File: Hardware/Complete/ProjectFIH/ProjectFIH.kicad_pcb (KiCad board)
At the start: 2 copper layers, 94 x 99.1 mm, 84 parts, among them J1 Conn_01x02_Male, J10 Payload LED, J2 Power, J3 Power LED, J4 MCU Fail LED, J5 Heater LED, J6 Heater, J7 UART, J8 AVR-ISP-10, J9 Payload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

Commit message: Small PCB optimization
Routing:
- net Net-(C5-Pad1): track 71.5 -> 68.6 mm

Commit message: Small corrections
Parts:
- added R27: 470, Resistor_SMD:R_0805_2012Metric_Pad1.15x1.40mm_HandSolder, F.Cu at (75.2, 81.5)
- DA1: value LM335 -> LM135
- R15, R21: value 4.2k -> 4.3k
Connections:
- D5 pad 2: IRQ -> Net-(D5-Pad2)
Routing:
- net IRQ: track 43.3 -> 39.5 mm
- net Net-(D5-Pad2): track 0.00 -> 2.30 mm
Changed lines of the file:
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@@
     (thickness 1.6)
     (drawings 4)
-    (tracks 794)
+    (tracks 796)
     (zones 0)
-    (modules 84)
-    (nets 85)
+    (modules 85)
+    (nets 86)
   )
   (page A4)
@@
   (net 83 "Net-(U8-Pad27)")
   (net 84 "Net-(U8-Pad28)")
+  (net 85 "Net-(D5-Pad2)")
   (net_class Default "This is the default net class."
     (clearance 0.2)
@@
     (add_net "Net-(D4-Pad1)")
     (add_net "Net-(D5-Pad1)")
+    (add_net "Net-(D5-Pad2)")
     (add_net "Net-(D6-Pad1)")
     (add_net "Net-(DA1-Pad1)")
@@
     (add_net Temperature)
   )
+  (module Resistor_SMD:R_0805_2012Metric_Pad1.15x1.40mm_HandSolder (layer F.Cu)
+    (at 75.175 81.534)
+    (descr "Resistor SMD 0805 (2012 Metric), square (rectangular) end terminal, IPC_7351 nominal with elongated pad for handsoldering. (Body size source: https://docs.google.com/spreadsheets/d/1BsfQQcO9C6DZCsRaXUlFlo91Tg2WpOkGARC1WS5S8t0/edit?usp=sharing), generated with kicad-footprint-generator")
+    (tags "resistor handsolder")
+    (attr smd)
+    (fp_text reference R27 (at 0 -1.65) (layer F.SilkS)
+      (effects (font (size 1 1) (thickness 0.15)))
+    )
+    (fp_text value 470 (at 0 1.65) (layer F.Fab)
+      (effects (font (size 1 1) (thickness 0.15)))
+    )
+    (fp_text user %R (at 0 0) (layer F.Fab)
+      (effects (font (size 0.5 0.5) (thickness 0.08)))
+    )
+    (fp_line (start -1 0.6) (end -1 -0.6) (layer F.Fab) (width 0.1))
+    (fp_line (start -1 -0.6) (end 1 -0.6) (layer F.Fab) (width 0.1))
+    (fp_line (start 1 -0.6) (end 1 0.6) (layer F.Fab) (width 0.1))
+    (fp_line (start 1 0.6) (end -1 0.6) (layer F.Fab) (width 0.1))
+    (fp_line (start -0.261252 -0.71) (end 0.261252 -0.71) (layer F.SilkS) (width 0.12))
+    (fp_line (start -0.261252 0.71) (end 0.261252 0.71) (layer F.SilkS) (width 0.12))
+    (fp_line (start -1.85 0.95) (end -1.85 -0.95) (layer F.CrtYd) (width 0.05))
+    (fp_line (start -1.85 -0.95) (end 1.85 -0.95) (layer F.CrtYd) (width 0.05))
+    (fp_line (start 1.85 -0.95) (end 1.85 0.95) (layer F.CrtYd) (width 0.05))
+    (fp_line (start 1.85 0.95) (end -1.85 0.95) (layer F.CrtYd) (width 0.05))
+    (pad 2 smd roundrect (at 1.025 0) (size 1.15 1.4) (layers F.Cu F.Paste F.Mask) (roundrect_rratio 0.217391)
+      (net 85 "Net-(D5-Pad2)"))
+    (pad 1 smd roundrect (at -1.025 0) (size 1.15 1.4) (layers F.Cu F.Paste F.Mask) (roundrect_rratio 0.217391)
+      (net 20 IRQ))
+    (model ${KISYS3DMOD}/Resistor_SMD.3dshapes/R_0805_2012Metric.wrl
+      (at (xyz 0 0 0))
+      (scale (xyz 1 1 1))
+      (rotate (xyz 0 0 0))
+    )
+  )
   (module Capacitor_SMD:C_0805_2012Metric_Pad1.15x1.40mm_HandSolder (layer F.Cu)
     (at 46.745 36.322)
@@
       (net 19 "Net-(D5-Pad1)"))
     (pad 2 smd roundrect (at 1.4 0 180) (size 1.25 2.65) (layers F.Cu F.Paste F.Mask) (roundrect_rratio 0.2)
-      (net 20 IRQ))
+      (net 85 "Net-(D5-Pad2)"))
     (model ${KISYS3DMOD}/Diode_SMD.3dshapes/D_1210_3225Metric.wrl
       (at (xyz 0 0 0))
@@
       (effects (font (size 1 1) (thickness 0.15)) (justify mirror))
     )
-    (fp_text value LM335 (at 1.27 -2.79) (layer B.Fab)
+    (fp_text value LM135 (at 1.27 -2.79) (layer B.Fab)
       (effects (font (size 1 1) (thickness 0.15)) (justify mirror))
     )
@@
       (effects (font (size 1 1) (thickness 0.15)))
     )
-    (fp_text value 4.2k (at 0 1.65 90) (layer F.Fab)
+    (fp_text value 4.3k (at 0 1.65 90) (layer F.Fab)
       (effects (font (size 1 1) (thickness 0.15)))
     )
@@
       (effects (font (size 1 1) (thickness 0.15)))
     )
-    (fp_text value 4.2k (at 0 1.65 90) (layer F.Fab)
+    (fp_text value 4.3k (at 0 1.65 90) (layer F.Fab)
       (effects (font (size 1 1) (thickness 0.15)))
     )
@@
   (segment (start 61.976 82.296) (end 61.976 82.296) (width 0.5) (layer B.Cu) (net 20))
   (via (at 61.976 82.296) (size 2.54) (drill 0.5) (layers F.Cu B.Cu) (net 20))
-  (segment (start 77.972 82.804) (end 74.676 82.804) (width 0.5) (layer F.Cu) (net 20))
-  (segment (start 74.676 82.804) (end 73.406 81.534) (width 0.5) (layer F.Cu) (net 20))
   (segment (start 62.738 81.534) (end 61.976 82.296) (width 0.5) (layer F.Cu) (net 20))
-  (segment (start 73.406 81.534) (end 62.738 81.534) (width 0.5) (layer F.Cu) (net 20))
   (segment (start 61.976 82.296) (end 61.976 77.978) (width 0.5) (layer F.Cu) (net 20))
+  (segment (start 72.898 81.534) (end 62.738 81.534) (width 0.5) (layer F.Cu) (net 20))
+  (segment (start 73.406 81.534) (end 72.898 81.534) (width 0.5) (layer F.Cu) (net 20))
+  (segment (start 72.898 81.534) (end 74.15 81.534) (width 0.5) (layer F.Cu) (net 20))
   (segment (start 100.457 21.965) (end 100.457 20.075) (width 1) (layer F.Cu) (net 21))
   (segment (start 100.457 20.075) (end 100.212 20.075) (width 1) (layer F.Cu) (net 21))
@@
   (segment (start 68.132001 89.601999) (end 67.564 90.17) (width 1) (layer B.Cu) (net 58))
   (segment (start 81.727999 89.601999) (end 75.625001 89.601999) (width 0.5) (layer B.Cu) (net 58))
+  (segment (start 77.47 82.804) (end 76.2 81.534) (width 0.5) (layer F.Cu) (net 85))
+  (segment (start 77.972 82.804) (end 77.47 82.804) (width 0.5) (layer F.Cu) (net 85))
   (zone (net 4) (net_name GND) (layer F.Cu) (hatch edge 0.508)
     (connect_pads (clearance 0.508))

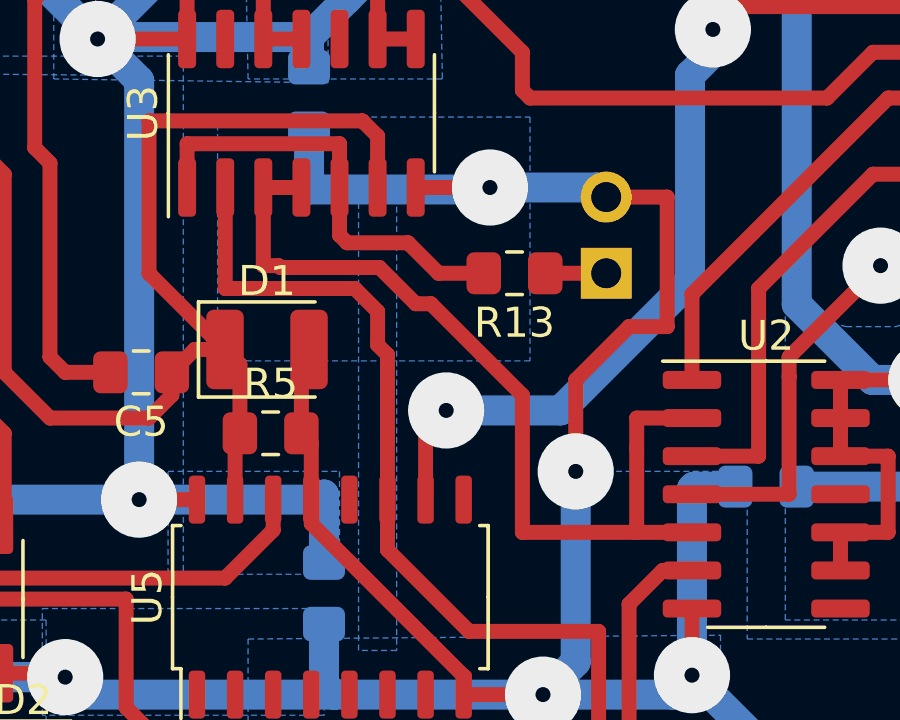
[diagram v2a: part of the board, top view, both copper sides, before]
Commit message: Swapped outputs of U3
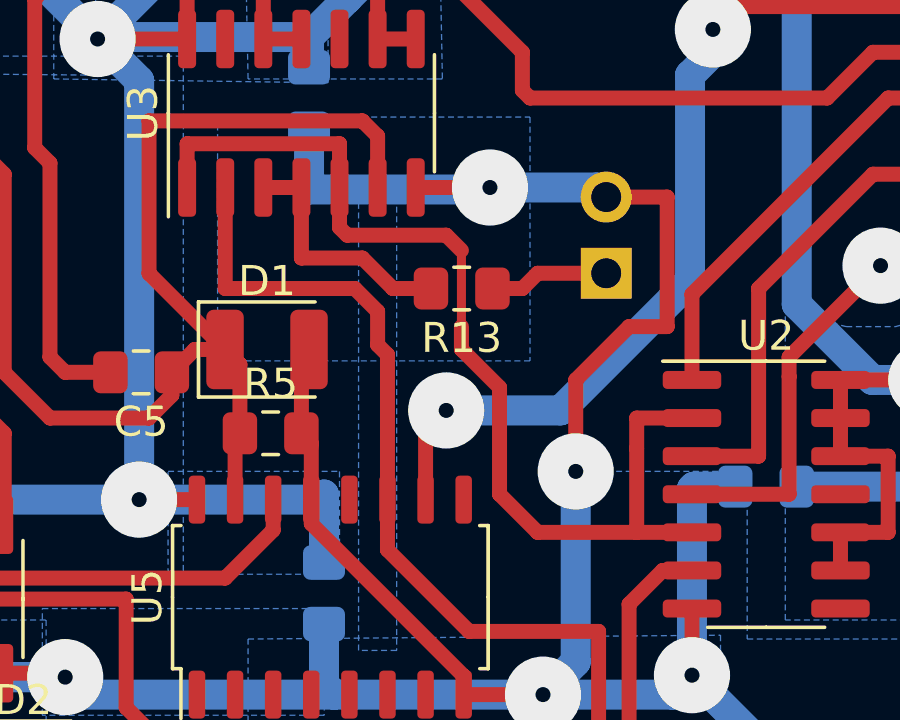
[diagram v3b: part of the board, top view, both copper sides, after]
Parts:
- moved R13 1.83 mm to (53.6, 90.9)
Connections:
- U3 pad 1: Net-(R13-Pad2) -> Net-(U2-Pad2)
- U3 pad 3: Net-(U2-Pad2) -> Net-(R13-Pad2)
- U3 pad 4: Net-(U2-Pad2) -> Net-(R13-Pad2)
- U3 pad 5: Net-(R13-Pad2) -> Net-(U2-Pad2)
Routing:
- net Net-(R13-Pad2): track 14.9 -> 8.36 mm
- net Net-(U2-Pad2): track 30.2 -> 35.0 mm
- net Net-(J4-Pad1): track 2.03 -> 4.00 mm

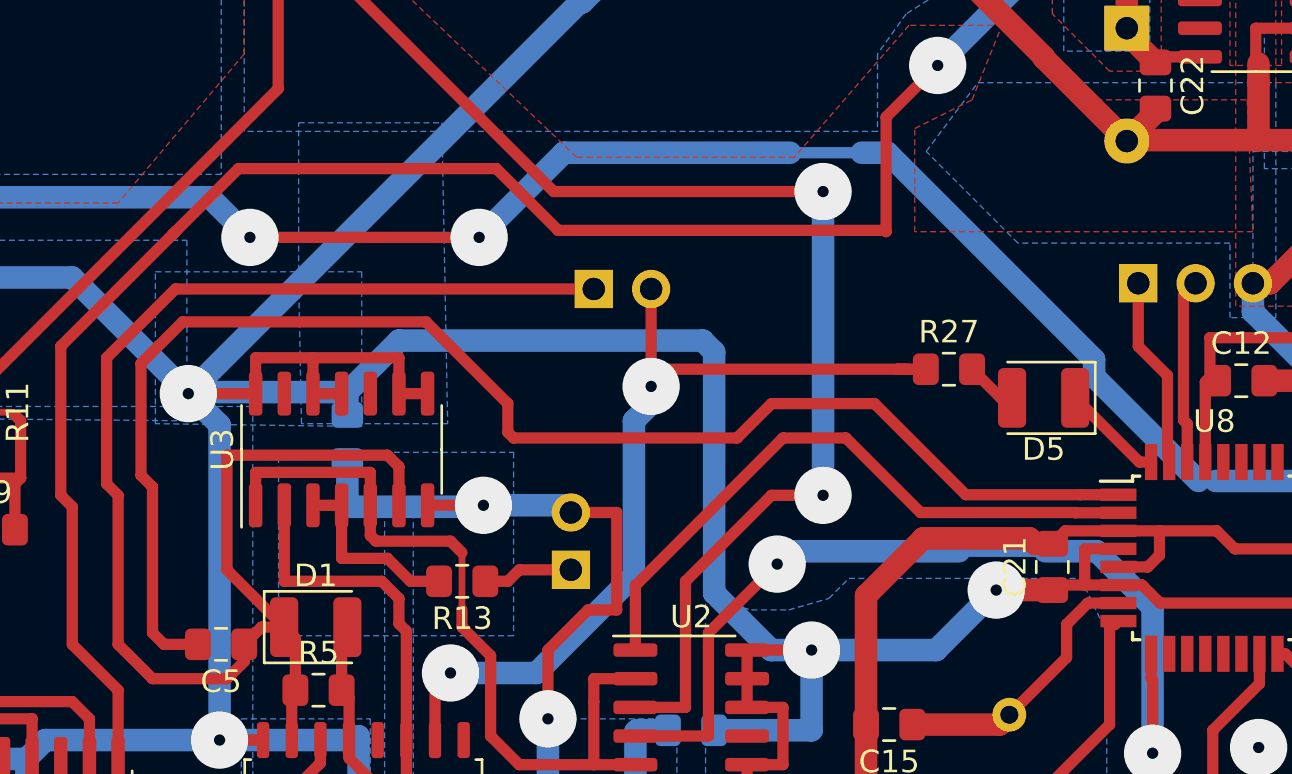
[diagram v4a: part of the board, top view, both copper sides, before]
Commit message: Important schematics and PCB fixes + some firmware development.
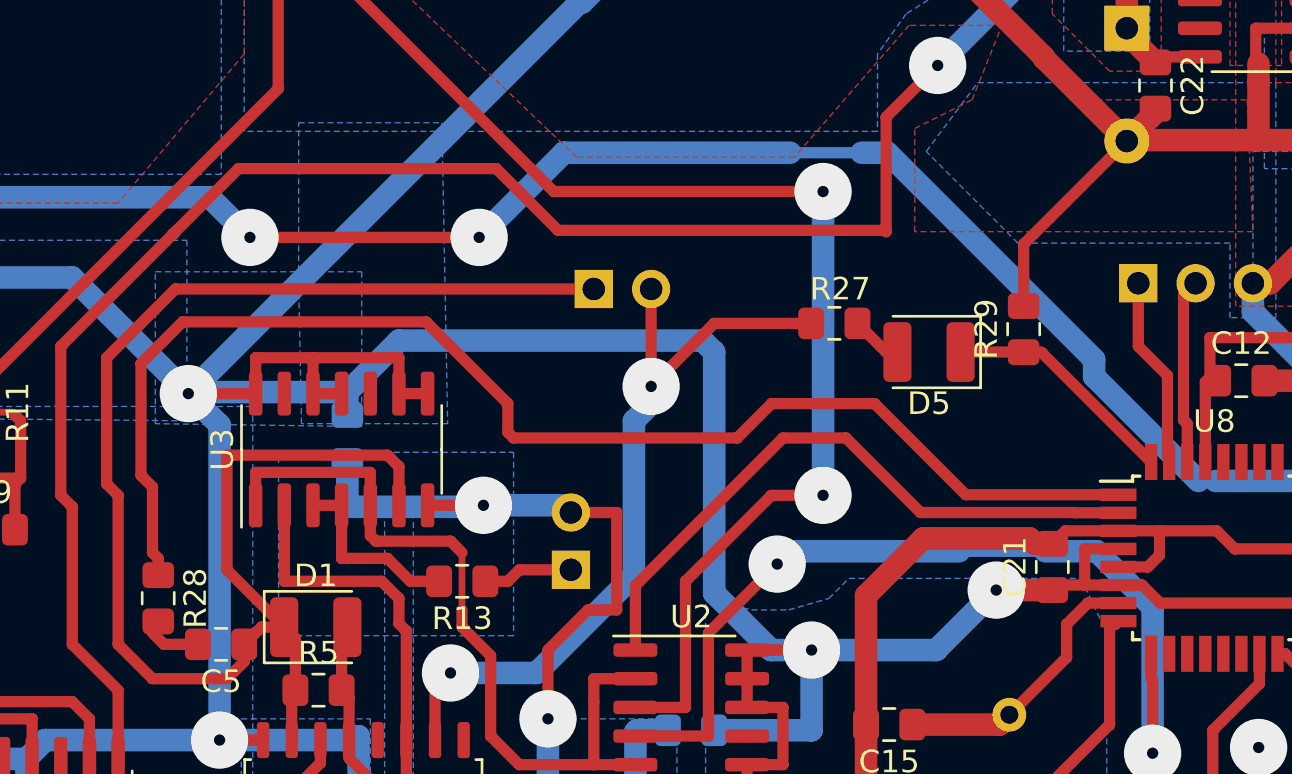
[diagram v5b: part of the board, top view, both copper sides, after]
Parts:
- added R28: 1k, Resistor_SMD:R_0805_2012Metric_Pad1.15x1.40mm_HandSolder, F.Cu at (40.1, 91.7)
- added R29: 10k, Resistor_SMD:R_0805_2012Metric_Pad1.15x1.40mm_HandSolder, F.Cu at (78.5, 79.8)
- R5: value 1k -> 10k
- moved R27 5.47 mm to (70.1, 79.5)
- moved D5 5.47 mm to (74.3, 80.8)
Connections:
- C5 pad 2: IRQResp -> Net-(C5-Pad2)
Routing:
- net GND: track 541.1 -> 550.3 mm
- net Net-(D5-Pad1): track 4.54 -> 10.5 mm
- net IRQ: track 39.5 -> 34.7 mm
- net IRQResp: track 63.6 -> 59.0 mm
- net Net-(C5-Pad2): track 0.00 -> 2.22 mm
